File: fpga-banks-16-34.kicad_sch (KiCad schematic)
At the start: 40 parts

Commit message: Added EN pullup for TPS54561 to avoid disabling by touch
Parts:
- C168, C169, C170, C171, C172, C173, C174, C175, C176: value (none) -> C_100n_0402_6V3; footprint (none) -> ddr5-testboard-footprints:0402-cap
- FB10, FB11, FB9: value (none) -> BLM15AG601SN1D; footprint (none) -> ddr5-testboard-footprints:0402-res
- J8: value (none) -> PinHeader_2x4; footprint (none) -> ddr5-testboard-footprints:PinHeader_2x04_P2.54mm_Vertical
- R124, R125, R128, R129, R159, R160: value (none) -> R_1k_0603; footprint (none) -> ddr5-testboard-footprints:0603-res
- R126, R127, R130, R131, R161, R162: value (none) -> R_120R_0603; footprint (none) -> ddr5-testboard-footprints:0603-res
- R132: value (none) -> R_200k_0402; footprint (none) -> ddr5-testboard-footprints:0402-res
- R133, R135, R136, R137, R138, R139, R140: value (none) -> R_0R_0402; footprint (none) -> ddr5-testboard-footprints:0402-res
- R171, R172, R173, R174: value (none) -> R_4k7_0402; footprint (none) -> ddr5-testboard-footprints:0402-res
- U13: value (none) -> ASFLMB-100.000MHZ-XY-T; footprint (none) -> ddr5-testboard-footprints:ASFLMB-100.000MHZ-XY-T
- U14: value (none) -> TCA39306DCUR; footprint (none) -> ddr5-testboard-footprints:VSSOP-8
- U8: value (none) -> XC7K160T-FFG676; footprint (none) -> ddr5-testboard-footprints:BGA676C100P26X26_2700X2700X254

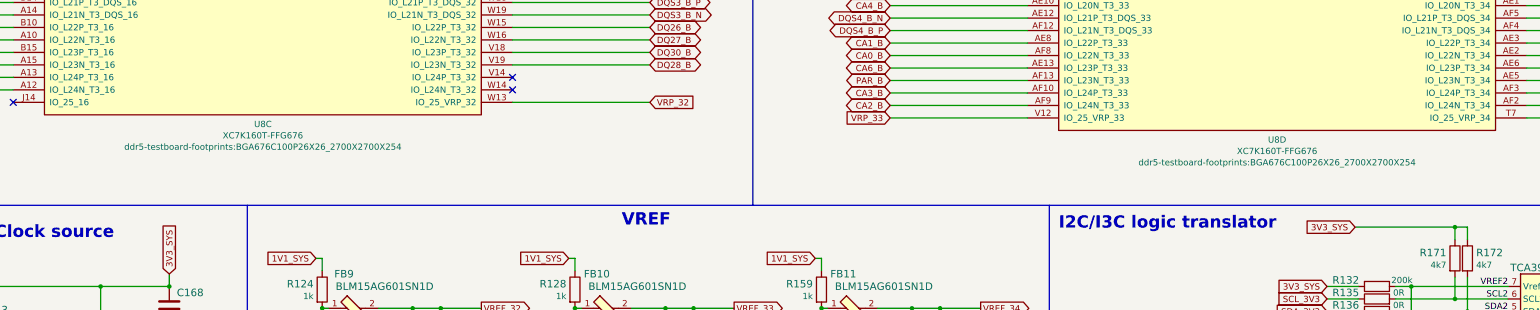
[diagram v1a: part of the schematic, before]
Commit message: Update FPGA footprint reference
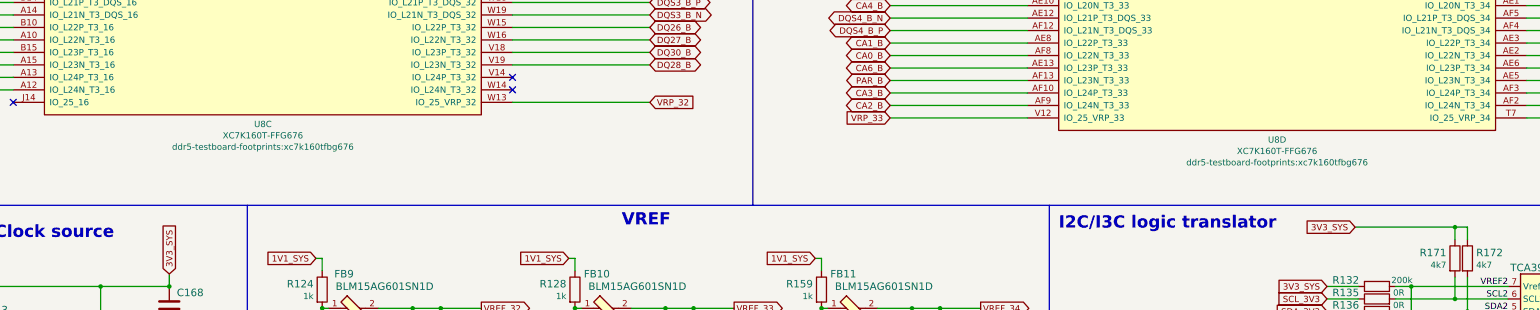
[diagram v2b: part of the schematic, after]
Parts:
- U8: footprint ddr5-testboard-footprints:BGA676C100P26X26_2700X2700X254 -> ddr5-testboard-footprints:xc7k160tfbg676
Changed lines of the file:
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@@
     (pin "2")
   )
-  (symbol (lib_id "ddr5-testboard:XC7K160T-FFG676") (at 96.52 129.54 0) (unit 3)
+  (symbol (lib_name "XC7K160T-FFG676_1") (lib_id "ddr5-testboard:XC7K160T-FFG676") (at 96.52 129.54 0) (unit 3)
     (in_bom yes) (on_board yes)
     (property "Reference" "U8" (id 0) (at 96.52 205.105 0))
     (property "Value" "XC7K160T-FFG676" (id 1) (at 96.52 207.4164 0))
-    (property "Footprint" "ddr5-testboard-footprints:BGA676C100P26X26_2700X2700X254" (id 2) (at 96.52 209.7278 0))
+    (property "Footprint" "ddr5-testboard-footprints:xc7k160tfbg676" (id 2) (at 96.52 209.7278 0))
     (property "Datasheet" "" (id 3) (at 96.52 129.54 0))
     (pin "AA21")
@@
     (property "Reference" "U8" (id 0) (at 302.895 208.28 0))
     (property "Value" "XC7K160T-FFG676" (id 1) (at 302.895 210.5914 0))
-    (property "Footprint" "ddr5-testboard-footprints:BGA676C100P26X26_2700X2700X254" (id 2) (at 302.895 212.9028 0))
+    (property "Footprint" "ddr5-testboard-footprints:xc7k160tfbg676" (id 2) (at 302.895 212.9028 0))
     (property "Datasheet" "" (id 3) (at 302.895 132.715 0))
     (pin "AA21")

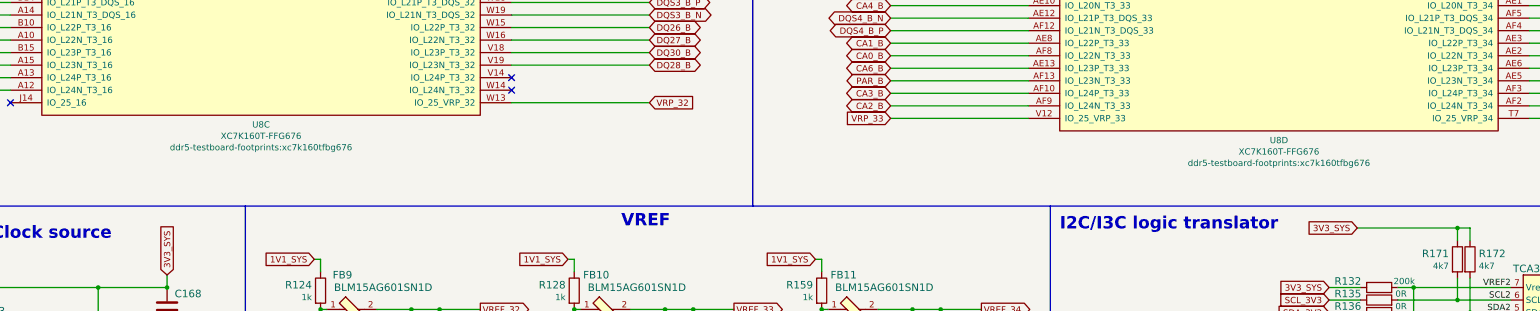
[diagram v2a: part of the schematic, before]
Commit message: Update naming convention
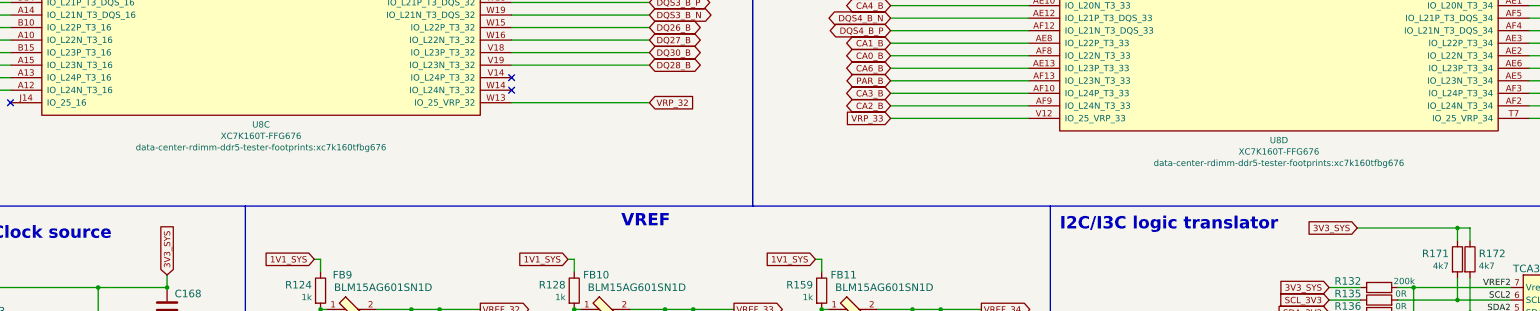
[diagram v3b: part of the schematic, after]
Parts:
- C168, C169, C170, C171, C172, C173, C174, C175, C176: footprint ddr5-testboard-footprints:0402-cap -> data-center-rdimm-ddr5-tester-footprints:0402-cap; symbol ddr5-testboard:C_100n_0402_6V3 -> data-center-rdimm-ddr5-tester:C_100n_0402_6V3
- FB10, FB11, FB9: footprint ddr5-testboard-footprints:0402-res -> data-center-rdimm-ddr5-tester-footprints:0402-res; symbol ddr5-testboard:BLM15AG601SN1D -> data-center-rdimm-ddr5-tester:BLM15AG601SN1D
- J8: footprint ddr5-testboard-footprints:PinHeader_2x04_P2.54mm_Vertical -> data-center-rdimm-ddr5-tester-footprints:PinHeader_2x04_P2.54mm_Vertical; symbol ddr5-testboard:PinHeader_2x4 -> data-center-rdimm-ddr5-tester:PinHeader_2x4
- R124, R125, R128, R129, R159, R160: footprint ddr5-testboard-footprints:0603-res -> data-center-rdimm-ddr5-tester-footprints:0603-res; symbol ddr5-testboard:R_1k_0603 -> data-center-rdimm-ddr5-tester:R_1k_0603
- R126, R127, R130, R131, R161, R162: footprint ddr5-testboard-footprints:0603-res -> data-center-rdimm-ddr5-tester-footprints:0603-res; symbol ddr5-testboard:R_120R_0603 -> data-center-rdimm-ddr5-tester:R_120R_0603
- R132: footprint ddr5-testboard-footprints:0402-res -> data-center-rdimm-ddr5-tester-footprints:0402-res; symbol ddr5-testboard:R_200k_0402 -> data-center-rdimm-ddr5-tester:R_200k_0402
- R133, R135, R136, R137, R138, R139, R140: footprint ddr5-testboard-footprints:0402-res -> data-center-rdimm-ddr5-tester-footprints:0402-res; symbol ddr5-testboard:R_0R_0402 -> data-center-rdimm-ddr5-tester:R_0R_0402
- R171, R172, R173, R174: footprint ddr5-testboard-footprints:0402-res -> data-center-rdimm-ddr5-tester-footprints:0402-res; symbol ddr5-testboard:R_4k7_0402 -> data-center-rdimm-ddr5-tester:R_4k7_0402
- U13: footprint ddr5-testboard-footprints:ASFLMB-100.000MHZ-XY-T -> data-center-rdimm-ddr5-tester-footprints:ASFLMB-100.000MHZ-XY-T; symbol ddr5-testboard:ASFLMB-100.000MHZ-XY-T -> data-center-rdimm-ddr5-tester:ASFLMB-100.000MHZ-XY-T
- U14: footprint ddr5-testboard-footprints:VSSOP-8 -> data-center-rdimm-ddr5-tester-footprints:VSSOP-8; symbol ddr5-testboard:TCA39306DCUR -> data-center-rdimm-ddr5-tester:TCA39306DCUR
- U8: footprint ddr5-testboard-footprints:xc7k160tfbg676 -> data-center-rdimm-ddr5-tester-footprints:xc7k160tfbg676; symbol ddr5-testboard:XC7K160T-FFG676 -> data-center-rdimm-ddr5-tester:XC7K160T-FFG676
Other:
- title: DDR5 Tester -> Data Center RDIMM DDR5 Tester

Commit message: Introduce component standarization
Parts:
- added unit 6 of U8
- added unit 8 of U8
- C168, C169, C170, C171, C172, C173, C174, C175, C176: value C_100n_0402_6V3 -> C_100n_6V3_0402; footprint data-center-rdimm-ddr5-tester-footprints:0402-cap -> data-center-rdimm-ddr5-tester-footprints:C_0402_1005Metric; symbol data-center-rdimm-ddr5-tester:C_100n_0402_6V3 -> data-center-rdimm-ddr5-tester:C_100n_6V3_0402; Author (none) -> Antmicro; License (none) -> Apache-2.0
- FB10, FB11, FB9: value BLM15AG601SN1D -> FB_600Z_0.3A_0402; footprint data-center-rdimm-ddr5-tester-footprints:0402-res -> data-center-rdimm-ddr5-tester-footprints:FB_0402_1005Metric; symbol data-center-rdimm-ddr5-tester:BLM15AG601SN1D -> data-center-rdimm-ddr5-tester:FB_600Z_0.3A_0402; Author (none) -> Antmicro; License (none) -> Apache-2.0
- J8: value PinHeader_2x4 -> PinHeader_2x4_P2.54mm_Drill1mm; footprint data-center-rdimm-ddr5-tester-footprints:PinHeader_2x04_P2.54mm_Vertical -> data-center-rdimm-ddr5-tester-footprints:PinHeader_2x4_P2.54mm_Drill1mm; symbol data-center-rdimm-ddr5-tester:PinHeader_2x4 -> data-center-rdimm-ddr5-tester:PinHeader_2x4_P2.54mm_Drill1mm; Author (none) -> Antmicro; License (none) -> Apache-2.0; MPN (none) -> SMH100-LPSE-D04-ST-BK; Manufacturer CNC Tech -> Sullins Connector Solutions
- R124, R125, R128, R129, R159, R160: footprint data-center-rdimm-ddr5-tester-footprints:0603-res -> data-center-rdimm-ddr5-tester-footprints:R_0603_1608Metric; Author (none) -> Antmicro; License (none) -> Apache-2.0; MPN CR0603-JW-102ELF -> CR0603-FX-1001ELF; Manufacturer BOURNS -> Bourns; Tolerance (none) -> 1%
- R126, R127, R130, R131, R161, R162: footprint data-center-rdimm-ddr5-tester-footprints:0603-res -> data-center-rdimm-ddr5-tester-footprints:R_0603_1608Metric; Author (none) -> Antmicro; License (none) -> Apache-2.0; MPN CRCW0603120RFKEA -> CR0603-FX-1200ELF; Manufacturer VISHAY -> Bourns; Tolerance (none) -> 1%
- R132: footprint data-center-rdimm-ddr5-tester-footprints:0402-res -> data-center-rdimm-ddr5-tester-footprints:R_0402_1005Metric; Author (none) -> Antmicro; License (none) -> Apache-2.0; MPN RC0402FR-07200KL -> CR0402-FX-2003GLF; Manufacturer YAGEO_(PHYCOMP) -> Bourns; Tolerance (none) -> 1%
- R133, R135, R136, R137, R138, R139, R140: footprint data-center-rdimm-ddr5-tester-footprints:0402-res -> data-center-rdimm-ddr5-tester-footprints:R_0402_1005Metric; Author (none) -> Antmicro; Current (none) -> 1A; License (none) -> Apache-2.0; Manufacturer PANASONIC -> Panasonic
- R171, R172, R173, R174: footprint data-center-rdimm-ddr5-tester-footprints:0402-res -> data-center-rdimm-ddr5-tester-footprints:R_0402_1005Metric; Author (none) -> Antmicro; License (none) -> Apache-2.0; MPN MCS04020C4701FE000 -> CR0402-FX-4701GLF; Manufacturer VISHAY -> Bourns; Tolerance (none) -> 1%
- U13: value ASFLMB-100.000MHZ-XY-T -> Oscillator_SMD_100MHz_ASFLMB; footprint data-center-rdimm-ddr5-tester-footprints:ASFLMB-100.000MHZ-XY-T -> data-center-rdimm-ddr5-tester-footprints:Oscillator_SMD_Abracon_ASFLMB_5x3.2x0.85mm; symbol data-center-rdimm-ddr5-tester:ASFLMB-100.000MHZ-XY-T -> data-center-rdimm-ddr5-tester:Oscillator_SMD_100MHz_ASFLMB; Author (none) -> Antmicro; License (none) -> Apache-2.0
- U14: value TCA39306DCUR -> TCA39306_VSSOP; footprint data-center-rdimm-ddr5-tester-footprints:VSSOP-8 -> data-center-rdimm-ddr5-tester-footprints:VSSOP-8_2.3x2mm_P0.5mm; symbol data-center-rdimm-ddr5-tester:TCA39306DCUR -> data-center-rdimm-ddr5-tester:TCA39306_VSSOP; Author (none) -> Antmicro; License (none) -> Apache-2.0
- U8: footprint data-center-rdimm-ddr5-tester-footprints:xc7k160tfbg676 -> data-center-rdimm-ddr5-tester-footprints:BGA-676_27x27mm_Layout26x26_P1X1mm; Author (none) -> Antmicro; License (none) -> Apache-2.0; MPN (none) -> XC7K160T-FFG676; Manufacturer (none) -> Xilinx
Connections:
- net 1V1_SYS: now also U8.AA1 (VCCO_34), U8.AB18 (VCCO_32), U8.AC15 (VCCO_32), U8.AC5 (VCCO_34), U8.AD2 (VCCO_34), U8.AE19 (VCCO_32), U8.AF16 (VCCO_32), U8.AF6 (VCCO_34), U8.U3 (VCCO_34), U8.W17 (VCCO_32), U8.Y14 (VCCO_32), U8.Y4 (VCCO_34); no longer U8.AA1 (VCCO_34), U8.AB18 (VCCO_32), U8.AC15 (VCCO_32), U8.AC5 (VCCO_34), U8.AD2 (VCCO_34), U8.AE19 (VCCO_32), U8.AF16 (VCCO_32), U8.AF6 (VCCO_34), U8.U3 (VCCO_34), U8.W17 (VCCO_32), U8.Y14 (VCCO_32), U8.Y4 (VCCO_34)
- net ALERT_N: now also U8.AF2 (IO_L24N_T3_34); no longer U8.AF2 (IO_L24N_T3_34)
- net CS0_A_N: now also U8.AA2 (IO_L12N_T1_MRCC_34); no longer U8.AA2 (IO_L12N_T1_MRCC_34)
- net CS1_A_N: now also U8.AA3 (IO_L12P_T1_MRCC_34); no longer U8.AA3 (IO_L12P_T1_MRCC_34)
- net DLBDQ: now also U8.AB16 (IO_L12P_T1_MRCC_32); no longer U8.AB16 (IO_L12P_T1_MRCC_32)
- net DLBDQS: now also U8.AC16 (IO_L12N_T1_MRCC_32); no longer U8.AC16 (IO_L12N_T1_MRCC_32)
- net DQ0_A: now also U8.U6 (IO_L1P_T0_34); no longer U8.U6 (IO_L1P_T0_34)
- net DQ0_B: now also U8.AF14 (IO_L2P_T0_32); no longer U8.AF14 (IO_L2P_T0_32)
- net DQ10_A: now also U8.V2 (IO_L8P_T1_34); no longer U8.V2 (IO_L8P_T1_34)
- net DQ10_B: now also U8.AD14 (IO_L8N_T1_32); no longer U8.AD14 (IO_L8N_T1_32)
- net DQ11_A: now also U8.Y1 (IO_L10N_T1_34); no longer U8.Y1 (IO_L10N_T1_34)
- net DQ11_B: now also U8.AA15 (IO_L7N_T1_32); no longer U8.AA15 (IO_L7N_T1_32)
- net DQ12_A: now also U8.Y2 (IO_L7N_T1_34); no longer U8.Y2 (IO_L7N_T1_34)
- net DQ12_B: now also U8.AB14 (IO_L10P_T1_32); no longer U8.AB14 (IO_L10P_T1_32)
- net DQ13_A: now also U8.Y3 (IO_L7P_T1_34); no longer U8.Y3 (IO_L7P_T1_34)
- net DQ13_B: now also U8.AA17 (IO_L11P_T1_SRCC_32); no longer U8.AA17 (IO_L11P_T1_SRCC_32)
- net DQ14_A: now also U8.AB2 (IO_L11P_T1_SRCC_34); no longer U8.AB2 (IO_L11P_T1_SRCC_34)
- net DQ14_B: now also U8.AB15 (IO_L10N_T1_32); no longer U8.AB15 (IO_L10N_T1_32)
- net DQ15_A: now also U8.AC2 (IO_L11N_T1_SRCC_34); no longer U8.AC2 (IO_L11N_T1_SRCC_34)
- net DQ15_B: now also U8.AA18 (IO_L11N_T1_SRCC_32); no longer U8.AA18 (IO_L11N_T1_SRCC_32)
- net DQ16_A: now also U8.Y5 (IO_L17N_T2_34); no longer U8.Y5 (IO_L17N_T2_34)
- net DQ16_B: now also U8.AD18 (IO_L13N_T2_MRCC_32); no longer U8.AD18 (IO_L13N_T2_MRCC_32)
- net DQ17_A: now also U8.AA4 (IO_L13P_T2_MRCC_34); no longer U8.AA4 (IO_L13P_T2_MRCC_34)
- net DQ17_B: now also U8.AD19 (IO_L17N_T2_32); no longer U8.AD19 (IO_L17N_T2_32)
- net DQ18_A: now also U8.Y6 (IO_L17P_T2_34); no longer U8.Y6 (IO_L17P_T2_34)
- net DQ18_B: now also U8.AC17 (IO_L14N_T2_SRCC_32); no longer U8.AC17 (IO_L14N_T2_SRCC_32)
- net DQ19_A: now also U8.AB4 (IO_L13N_T2_MRCC_34); no longer U8.AB4 (IO_L13N_T2_MRCC_34)
- net DQ19_B: now also U8.AC18 (IO_L13P_T2_MRCC_32); no longer U8.AC18 (IO_L13P_T2_MRCC_32)
- net DQ1_A: now also U8.U5 (IO_L1N_T0_34); no longer U8.U5 (IO_L1N_T0_34)
- net DQ1_B: now also U8.AE15 (IO_L4N_T0_32); no longer U8.AE15 (IO_L4N_T0_32)
- net DQ20_A: now also U8.AB6 (IO_L16P_T2_34); no longer U8.AB6 (IO_L16P_T2_34)
- net DQ20_B: now also U8.AB17 (IO_L14P_T2_SRCC_32); no longer U8.AB17 (IO_L14P_T2_SRCC_32)
- net DQ21_A: now also U8.AC4 (IO_L14P_T2_SRCC_34); no longer U8.AC4 (IO_L14P_T2_SRCC_34)
- net DQ21_B: now also U8.AA19 (IO_L16P_T2_32); no longer U8.AA19 (IO_L16P_T2_32)
- net DQ22_A: now also U8.AC3 (IO_L14N_T2_SRCC_34); no longer U8.AC3 (IO_L14N_T2_SRCC_34)
- net DQ22_B: now also U8.AC19 (IO_L17P_T2_32); no longer U8.AC19 (IO_L17P_T2_32)
- net DQ23_A: now also U8.AC6 (IO_L16N_T2_34); no longer U8.AC6 (IO_L16N_T2_34)
- net DQ23_B: now also U8.AA20 (IO_L16N_T2_32); no longer U8.AA20 (IO_L16N_T2_32)
- net DQ24_A: now also U8.AE3 (IO_L22P_T3_34); no longer U8.AE3 (IO_L22P_T3_34)
- net DQ24_B: now also U8.AB20 (IO_L18N_T2_32); no longer U8.AB20 (IO_L18N_T2_32)
- net DQ25_A: now also U8.AE2 (IO_L22N_T3_34); no longer U8.AE2 (IO_L22N_T3_34)
- net DQ25_B: now also U8.Y17 (IO_L19P_T3_32); no longer U8.Y17 (IO_L19P_T3_32)
- net DQ26_A: now also U8.AD1 (IO_L20P_T3_34); no longer U8.AD1 (IO_L20P_T3_34)
- net DQ26_B: now also U8.W15 (IO_L22P_T3_32); no longer U8.W15 (IO_L22P_T3_32)
- net DQ27_A: now also U8.AE1 (IO_L20N_T3_34); no longer U8.AE1 (IO_L20N_T3_34)
- net DQ27_B: now also U8.W16 (IO_L22N_T3_32); no longer U8.W16 (IO_L22N_T3_32)
- net DQ28_A: now also U8.AD4 (IO_L19P_T3_34); no longer U8.AD4 (IO_L19P_T3_34)
- net DQ28_B: now also U8.V19 (IO_L23N_T3_32); no longer U8.V19 (IO_L23N_T3_32)
- net DQ29_A: now also U8.AD5 (IO_L18N_T2_34); no longer U8.AD5 (IO_L18N_T2_34)
- net DQ29_B: now also U8.V17 (IO_L20N_T3_32); no longer U8.V17 (IO_L20N_T3_32)
- net DQ2_A: now also U8.U7 (IO_L5P_T0_34); no longer U8.U7 (IO_L5P_T0_34)
- net DQ2_B: now also U8.AF15 (IO_L2N_T0_32); no longer U8.AF15 (IO_L2N_T0_32)
- net DQ30_A: now also U8.AE5 (IO_L23N_T3_34); no longer U8.AE5 (IO_L23N_T3_34)
- net DQ30_B: now also U8.V18 (IO_L23P_T3_32); no longer U8.V18 (IO_L23P_T3_32)
- net DQ31_A: now also U8.AE6 (IO_L23P_T3_34); no longer U8.AE6 (IO_L23P_T3_34)
- net DQ31_B: now also U8.V16 (IO_L20P_T3_32); no longer U8.V16 (IO_L20P_T3_32)
- net DQ3_A: now also U8.V6 (IO_L5N_T0_34); no longer U8.V6 (IO_L5N_T0_34)
- net DQ3_B: now also U8.AF17 (IO_L1N_T0_32); no longer U8.AF17 (IO_L1N_T0_32)
- net DQ4_A: now also U8.U1 (IO_L2N_T0_34); no longer U8.U1 (IO_L2N_T0_34)
- net DQ4_B: now also U8.AE17 (IO_L1P_T0_32); no longer U8.AE17 (IO_L1P_T0_32)
- net DQ5_A: now also U8.V3 (IO_L4P_T0_34); no longer U8.V3 (IO_L4P_T0_34)
- net DQ5_B: now also U8.AD15 (IO_L4P_T0_32); no longer U8.AD15 (IO_L4P_T0_32)
- net DQ6_A: now also U8.U2 (IO_L2P_T0_34); no longer U8.U2 (IO_L2P_T0_34)
- net DQ6_B: now also U8.AF19 (IO_L5P_T0_32); no longer U8.AF19 (IO_L5P_T0_32)
- net DQ7_A: now also U8.W3 (IO_L4N_T0_34); no longer U8.W3 (IO_L4N_T0_34)
- net DQ7_B: now also U8.AF20 (IO_L5N_T0_32); no longer U8.AF20 (IO_L5N_T0_32)
- net DQ8_A: now also U8.V1 (IO_L8N_T1_34); no longer U8.V1 (IO_L8N_T1_34)
- net DQ8_B: now also U8.AC14 (IO_L8P_T1_32); no longer U8.AC14 (IO_L8P_T1_32)
- net DQ9_A: now also U8.W1 (IO_L10P_T1_34); no longer U8.W1 (IO_L10P_T1_34)
- net DQ9_B: now also U8.AA14 (IO_L7P_T1_32); no longer U8.AA14 (IO_L7P_T1_32)
- net DQS0_A_N: now also U8.W5 (IO_L3N_T0_DQS_34); no longer U8.W5 (IO_L3N_T0_DQS_34)
- net DQS0_A_P: now also U8.W6 (IO_L3P_T0_DQS_34); no longer U8.W6 (IO_L3P_T0_DQS_34)
- net DQS0_B_N: now also U8.AF18 (IO_L3N_T0_DQS_32); no longer U8.AF18 (IO_L3N_T0_DQS_32)
- net DQS0_B_P: now also U8.AE18 (IO_L3P_T0_DQS_32); no longer U8.AE18 (IO_L3P_T0_DQS_32)
- net DQS1_A_N: now also U8.AC1 (IO_L9N_T1_DQS_34); no longer U8.AC1 (IO_L9N_T1_DQS_34)
- net DQS1_A_P: now also U8.AB1 (IO_L9P_T1_DQS_34); no longer U8.AB1 (IO_L9P_T1_DQS_34)
- net DQS1_B_N: now also U8.Y16 (IO_L9N_T1_DQS_32); no longer U8.Y16 (IO_L9N_T1_DQS_32)
- net DQS1_B_P: now also U8.Y15 (IO_L9P_T1_DQS_32); no longer U8.Y15 (IO_L9P_T1_DQS_32)
- net DQS2_A_N: now also U8.AB5 (IO_L15N_T2_DQS_34); no longer U8.AB5 (IO_L15N_T2_DQS_34)
- net DQS2_A_P: now also U8.AA5 (IO_L15P_T2_DQS_34); no longer U8.AA5 (IO_L15P_T2_DQS_34)
- net DQS2_B_N: now also U8.AE20 (IO_L15N_T2_DQS_32); no longer U8.AE20 (IO_L15N_T2_DQS_32)
- net DQS2_B_P: now also U8.AD20 (IO_L15P_T2_DQS_32); no longer U8.AD20 (IO_L15P_T2_DQS_32)
- net DQS3_A_N: now also U8.AF4 (IO_L21N_T3_DQS_34); no longer U8.AF4 (IO_L21N_T3_DQS_34)
- net DQS3_A_P: now also U8.AF5 (IO_L21P_T3_DQS_34); no longer U8.AF5 (IO_L21P_T3_DQS_34)
- net DQS3_B_N: now also U8.W19 (IO_L21N_T3_DQS_32); no longer U8.W19 (IO_L21N_T3_DQS_32)
- net DQS3_B_P: now also U8.W18 (IO_L21P_T3_DQS_32); no longer U8.W18 (IO_L21P_T3_DQS_32)
- net RESET_N: now also U8.AF3 (IO_L24P_T3_34); no longer U8.AF3 (IO_L24P_T3_34)
- net VREF_32: now also U8.AE16 (IO_L6N_T0_VREF_32), U8.Y18 (IO_L19N_T3_VREF_32); no longer U8.AE16 (IO_L6N_T0_VREF_32), U8.Y18 (IO_L19N_T3_VREF_32)
- net VREF_34: now also U8.AD3 (IO_L19N_T3_VREF_34), U8.W4 (IO_L6N_T0_VREF_34); no longer U8.AD3 (IO_L19N_T3_VREF_34), U8.W4 (IO_L6N_T0_VREF_34)
- net VRN_32: now also U8.V13 (IO_0_VRN_32); no longer U8.V13 (IO_0_VRN_32)
- net VRN_34: now also U8.U4 (IO_0_VRN_34); no longer U8.U4 (IO_0_VRN_34)
- net VRP_32: now also U8.W13 (IO_25_VRP_32); no longer U8.W13 (IO_25_VRP_32)
- net VRP_34: now also U8.T7 (IO_25_VRP_34); no longer U8.T7 (IO_25_VRP_34)
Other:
- note removed: "IC2"
- moved on the sheet: C168, C169, C170, C171, C172, C173, C174, C175, C176, J8, R124, R125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

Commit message: [#55296] component update
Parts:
- J8: footprint data-center-rdimm-ddr5-tester-footprints:PinHeader_2x4_P2.54mm_Drill1mm -> antmicro-footprints:PinHeader_2x4_P2.54mm_Drill1.1mm; symbol data-center-rdimm-ddr5-tester:PinHeader_2x4_P2.54mm_Drill1mm -> data-center-rdimm-ddr5-tester:PinHeader_2x4_P2.54mm_Drill1.1mm; MPN SMH100-LPSE-D04-ST-BK -> 62000821121; Manufacturer Sullins Connector Solutions -> Würth Elektronik; now not fitted; now left out of the parts list
- U13: symbol data-center-rdimm-ddr5-tester:Oscillator_SMD_100MHz_ASFLMB -> data-center-rdimm-ddr5-tester:Oscillator_100MHz_ASFLMB; Val (none) -> 100 MHz
- U8: Manufacturer Xilinx -> AMD-Xilinx
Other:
- moved on the sheet: C168
